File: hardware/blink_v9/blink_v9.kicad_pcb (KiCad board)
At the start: 2 copper layers, 119 x 92 mm, 115 parts, among them J1 Conn_01x02, J11 KH-BNC50-3511, J12 KH-BNC50-3511, J13 KH-BNC50-3511, J14 Conn_02x16_Odd_Even, J15 Conn_01x01, J16 Conn_01x01, J2 PJ-320D, J3 PJ-320D, J4 KH-BNC50-3511, J5 Conn_01x06_Pin, J7 Conn_01x06_Pin, J8 Conn_01x06, J9 USB_C_Receptacle, Q1 S8550, Q2 S8050, SW1 SW_SPDT, SW2 LC1258OASP, SW3 LC1258OASP, SW5 LC1258OASP, U1 AMS1117-3.3, U2 AD8397, U3 M24C02-RMN, U4 STM32F405RGTx, U5 SN74LVC1G14DBV, U6 SN74LVC1G14DBV, U7 CH340C, U8 USBLC6-2P6, U9 MCP73832-2-OT, X1 GTXO-14V (2.048MHz), Y1 16MHz

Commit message: fix up osc footprint
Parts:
- removed J8: Conn_01x06, Connector_JST:JST_PH_S6B-PH-SM4-TB_1x06-1MP_P2.00mm_Horizontal
- added C30: 100n, Capacitor_SMD:C_0402_1005Metric, F.Cu at (166.0, 33.0)
- added J6: Conn_01x03, Connector_JST:JST_PH_S3B-PH-SM4-TB_1x03-1MP_P2.00mm_Horizontal, F.Cu at (170.7, 26.4)
- added R42: 1K0, Resistor_SMD:R_0603_1608Metric, F.Cu at (178.8, 22.0)
- added R43: 1K0, Resistor_SMD:R_0603_1608Metric, F.Cu at (178.8, 24.5)
- added R44: 1K0, Resistor_SMD:R_0603_1608Metric, F.Cu at (178.8, 27.0)
- added R45: 1K0, Resistor_SMD:R_0603_1608Metric, F.Cu at (178.8, 29.5)
- added U10: TMP102xxDRL, Package_TO_SOT_SMD:SOT-563, F.Cu at (178.7, 32.4)
- Q1, Q2: footprint Package_TO_SOT_SMD:SC-59 -> Package_TO_SOT_THT:TO-92_Inline
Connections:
- net SYNC_IN2 renamed AUX_SYNC_IN
- J7 pad 2: /BOOT0 -> Net-(J7-Pin_2)
- J7 pad 3: /BOOT1 -> Net-(J7-Pin_3)
- J7 pad 4: /BTN1 -> Net-(J7-Pin_4)
- J7 pad 5: /DB3 -> Net-(J7-Pin_5)
- R35 pad 2: /BOOT0 -> /AUX_CLK
- U4 pad 42: /NCOL1 -> /USB_RX
- U4 pad 43: /LEDMY -> /USB_TX
- U4 pad 58: /USB_RX -> /NCOL1
- U4 pad 59: /USB_TX -> /LEDMY
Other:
- board text added: "Blink Rev 9.0 Cullen Jennings 2023"
- board text removed: "Blink Rev 8.0 Cullen Jennings 2023"

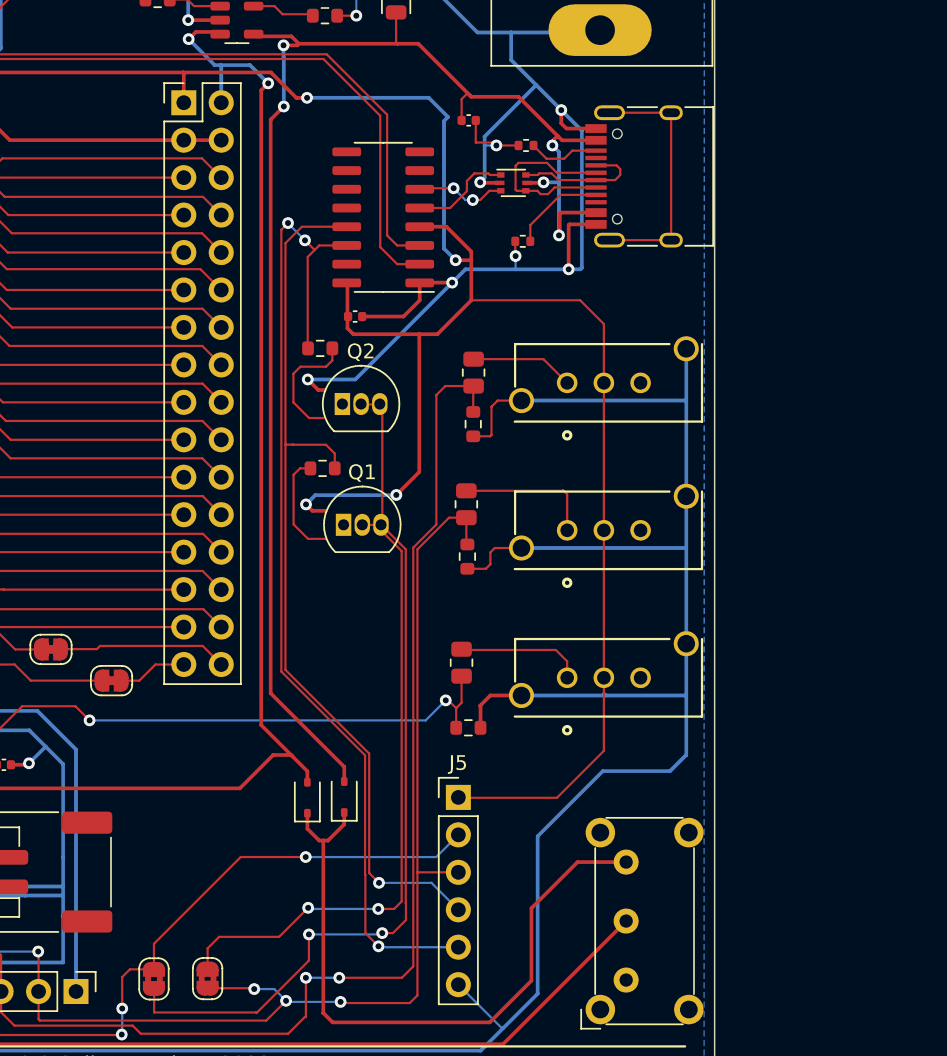
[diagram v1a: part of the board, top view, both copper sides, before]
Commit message: moved switches
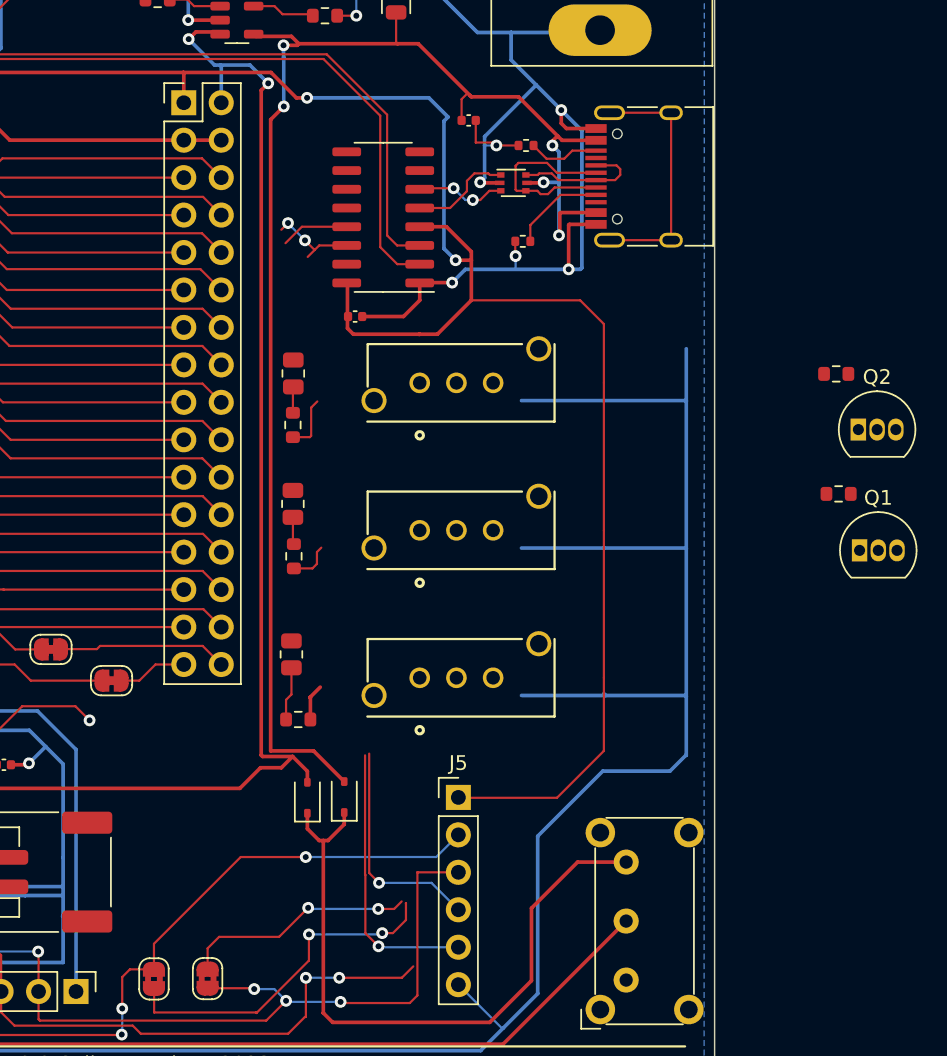
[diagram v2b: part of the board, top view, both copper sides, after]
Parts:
- moved Q1 35.0 mm to (239.8, 91.4)
- moved Q2 35.0 mm to (239.7, 83.2)
- moved R37 35.0 mm to (238.2, 79.4)
- moved R38 35.0 mm to (238.4, 87.5)
- moved R18 12.2 mm to (201.4, 82.9)
- moved R25 12.2 mm to (201.4, 79.4)
- moved R14 11.8 mm to (201.5, 91.8)
- moved R35 11.8 mm to (201.4, 88.2)
- moved R34 11.6 mm to (201.8, 102.8)
- moved R36 11.6 mm to (201.3, 98.4)
- moved SW2 10.0 mm to (210.0, 90.0)
- moved SW3 10.0 mm to (210.0, 100.0)
- moved SW5 10.0 mm to (210.0, 80.0)
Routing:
- net /USB_RTS: track 69.2 -> 25.0 mm
- net /BOOT1: track 126.4 -> 84.3 mm
- net /USB_DTR: track 61.4 -> 19.8 mm
- net Net-(JP3-B): track 59.2 -> 23.5 mm
- net Net-(JP4-B): track 43.2 -> 15.9 mm
- net /BOOT0: track 144.9 -> 118.8 mm
- net /BTN1: track 110.8 -> 85.1 mm, vias 5 -> 4
- net GND: track 1099.5 -> 1080.0 mm, vias 43 -> 42
- net +3.3V: track 507.6 -> 488.1 mm, vias 21 -> 19
- net Net-(R35-Pad1): track 9.41 -> 0.00 mm
- net Net-(R36-Pad1): track 8.62 -> 0.07 mm
- net Net-(Q2-B): track 8.34 -> 0.00 mm
- net Net-(Q1-B): track 7.28 -> 0.00 mm
- net Net-(R25-Pad1): track 7.01 -> 0.00 mm
- net VBUS: track 97.3 -> 99.0 mm
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
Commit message: place parts on v9
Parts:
- Q1, Q2: footprint Package_TO_SOT_THT:TO-92_Inline -> Package_TO_SOT_SMD:SOT-23-3
- X1: footprint blinky_footprints:Oscillator_DIP-14 -> blinky_footprints:OSC_DIP-14
- moved R42 93.6 mm to (177.2, 115.6), turned to -90 degrees
- moved R44 88.8 mm to (174.4, 115.7), turned to -90 degrees
- moved R43 88.0 mm to (175.6, 112.4), turned to -90 degrees
- moved R45 83.2 mm to (173.2, 112.5), turned to -90 degrees
- moved U10 68.5 mm to (158.6, 97.9), turned to 180 degrees
- moved C30 65.6 mm to (156.2, 97.8)
- moved Q1 54.6 mm to (204.5, 49.6)
- moved R38 54.6 mm to (203.1, 45.8)
- moved Q2 53.8 mm to (197.5, 49.8)
- moved R37 53.8 mm to (196.0, 46.0)
- moved J6 23.2 mm to (172.0, 49.5), turned to 180 degrees
- moved J1 2.15 mm to (186.7, 112.7)
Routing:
- net /BOOT1: track 84.3 -> 24.5 mm, vias 4 -> 2
- net Net-(J7-Pin_3): track 0.00 -> 46.3 mm, vias 0 -> 2
- net /DB3: track 54.3 -> 43.3 mm
- net Net-(J7-Pin_2): track 0.00 -> 10.7 mm
- net Net-(J7-Pin_5): track 0.00 -> 10.4 mm
- net /BTN1: track 85.1 -> 76.4 mm
- net GND: track 1080.0 -> 1071.4 mm
- net Net-(J7-Pin_4): track 0.00 -> 8.36 mm
- net Net-(J4-In): track 86.3 -> 92.2 mm
- net +BATT: track 95.1 -> 89.9 mm
- net /SWDCLK: track 42.1 -> 38.8 mm
- net /SWDIO: track 32.5 -> 29.3 mm
- net /USB_RX: track 99.9 -> 97.1 mm
- net +3.3V: track 488.1 -> 485.3 mm
- net +3.3VA: track 115.5 -> 118.1 mm
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
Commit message: add labels blink 9
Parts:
- moved J5 70.0 mm to (179.0, 46.7), turned to 90 degrees
- moved D2 12.1 mm to (213.8, 112.1)
- moved D3 12.1 mm to (216.3, 112.0)
- moved J6 6.72 mm to (165.3, 50.0)
- moved R18 2.60 mm to (204.0, 82.7)
- moved R25 2.60 mm to (204.0, 79.2)
- moved R35 2.21 mm to (203.6, 88.1)
- moved R14 2.21 mm to (203.7, 91.7)
- moved R34 2.12 mm to (203.8, 103.4)
- moved R36 2.12 mm to (203.3, 99.0)
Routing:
- net /USB_RX: track 97.1 -> 46.0 mm, vias 5 -> 1
- net /NCOL1: track 42.1 -> 88.6 mm, vias 0 -> 3
- net Net-(D2-K): track 45.0 -> 16.2 mm
- net /BOOT0: track 118.8 -> 95.9 mm, vias 5 -> 2
- net +3.3V: track 485.3 -> 465.2 mm, vias 19 -> 18
- net /USB_RTS: track 25.0 -> 6.19 mm, vias 3 -> 2
- net /USB_DTR: track 19.8 -> 4.62 mm, vias 1 -> 0
- net /NRST: track 112.5 -> 97.7 mm, vias 7 -> 6
- net VBUS: track 99.0 -> 112.7 mm
- net +BATT: track 89.9 -> 101.6 mm
- net Net-(JP3-B): track 23.5 -> 13.6 mm, vias 2 -> 0
- net Net-(J7-Pin_3): track 46.3 -> 38.7 mm, vias 2 -> 0
- net Net-(JP4-B): track 15.9 -> 9.36 mm, vias 2 -> 0
- net Net-(J4-In): track 92.2 -> 89.5 mm, vias 2 -> 1
- net /SWDIO: track 29.3 -> 27.9 mm, vias 2 -> 1
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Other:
- board text added: "BTN1"
- board text added: "BTN2"
- board text added: "BTN3"
- board text added: "Bat"
- board text added: "Debug"
- board text added: "MIC"
- board text added: "Prog"
- board text added: "SPKR"
- board text added: "SYNC IN"
- board text added: "SYNC OUT"

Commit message: fix up SMD sizes to motly 0603 on blink
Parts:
- C13, C17, C25, C26, C6, C7, C8, C9: footprint Capacitor_SMD:C_0805_2012Metric -> Capacitor_SMD:C_0603_1608Metric
- C28, C29: footprint Capacitor_SMD:C_0402_1005Metric -> Capacitor_SMD:C_0603_1608Metric
- R1, R13, R16, R19, R2, R24, R25, R3, R35, R36, R39, R4, R5, R6, R7, R8: footprint Resistor_SMD:R_0805_2012Metric -> Resistor_SMD:R_0603_1608Metric
- R21, R22: footprint Resistor_SMD:R_0402_1005Metric -> Resistor_SMD:R_0603_1608Metric
- moved R22 0.42 mm to (217.3, 70.2)
- moved R21 0.29 mm to (217.0, 63.7)
- moved C29 0.25 mm to (181.6, 105.9)
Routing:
- net (no net): track 0.00 -> 16.4 mm
- net GND: track 1070.3 -> 1075.0 mm
- net +BATT: track 101.6 -> 105.0 mm
- net Net-(U7-UD+): track 6.93 -> 8.54 mm
- net Net-(J9-CC1): track 6.40 -> 5.88 mm
- net Net-(U7-UD-): track 6.12 -> 5.68 mm, vias 2 -> 0

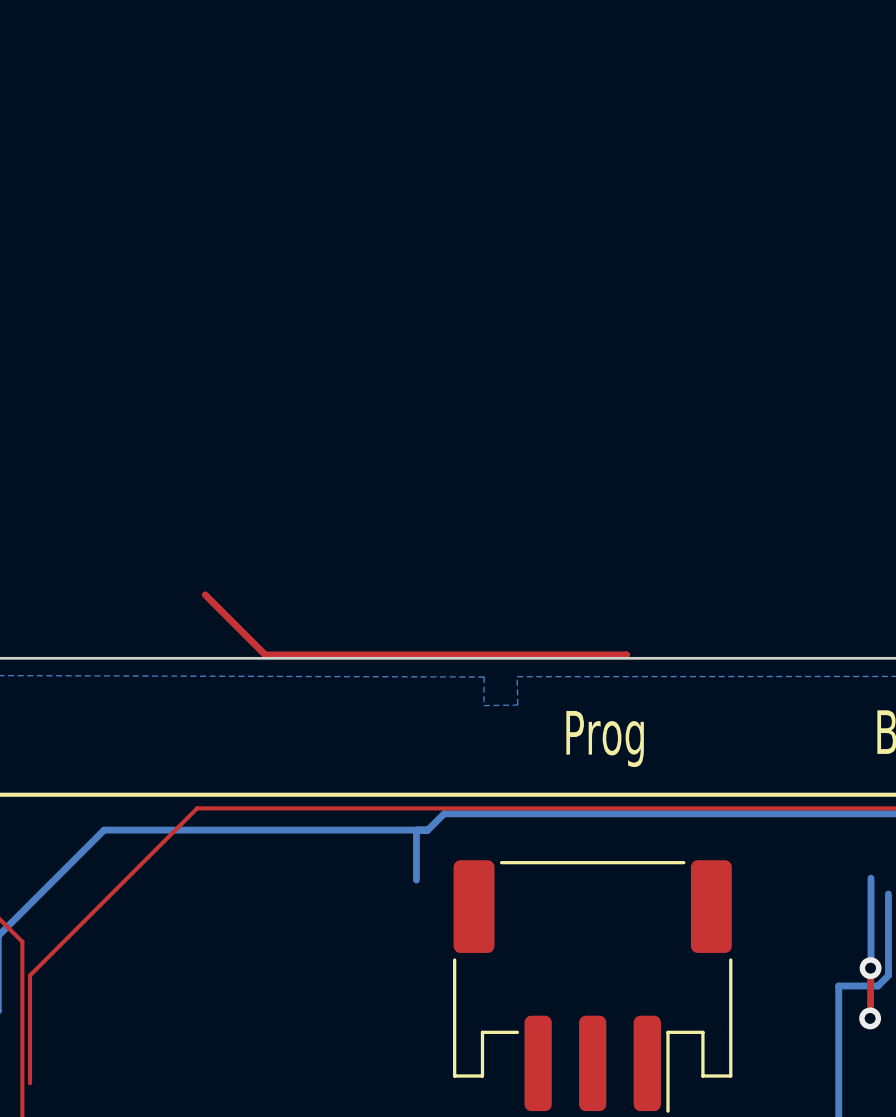
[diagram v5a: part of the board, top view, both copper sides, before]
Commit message: add RGB led
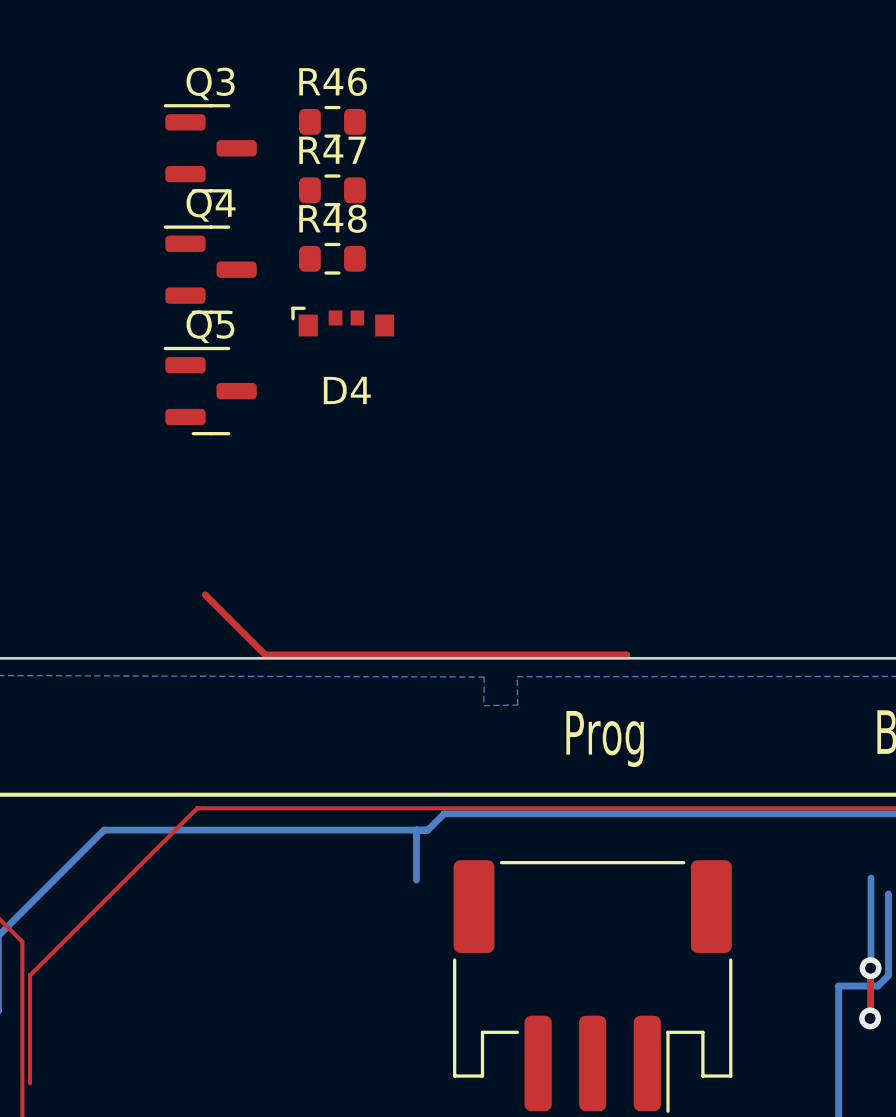
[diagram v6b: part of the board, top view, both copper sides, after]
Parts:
- added D4: LED_ABGR, blinky_footprints:LED_RGB_MHS110FRGBCT, F.Cu at (156.3, 26.4)
- added Q3: 2N7002, Package_TO_SOT_SMD:SOT-23, F.Cu at (151.3, 19.3)
- added Q4: 2N7002, Package_TO_SOT_SMD:SOT-23, F.Cu at (151.3, 23.8)
- added Q5: 2N7002, Package_TO_SOT_SMD:SOT-23, F.Cu at (151.3, 28.2)
- added R46: 150R, Resistor_SMD:R_0603_1608Metric, F.Cu at (155.8, 18.3)
- added R47: 47R, Resistor_SMD:R_0603_1608Metric, F.Cu at (155.8, 20.8)
- added R48: 47R, Resistor_SMD:R_0603_1608Metric, F.Cu at (155.8, 23.4)
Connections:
- R25 pad 1: Net-(R25-Pad1) -> /BOOT1

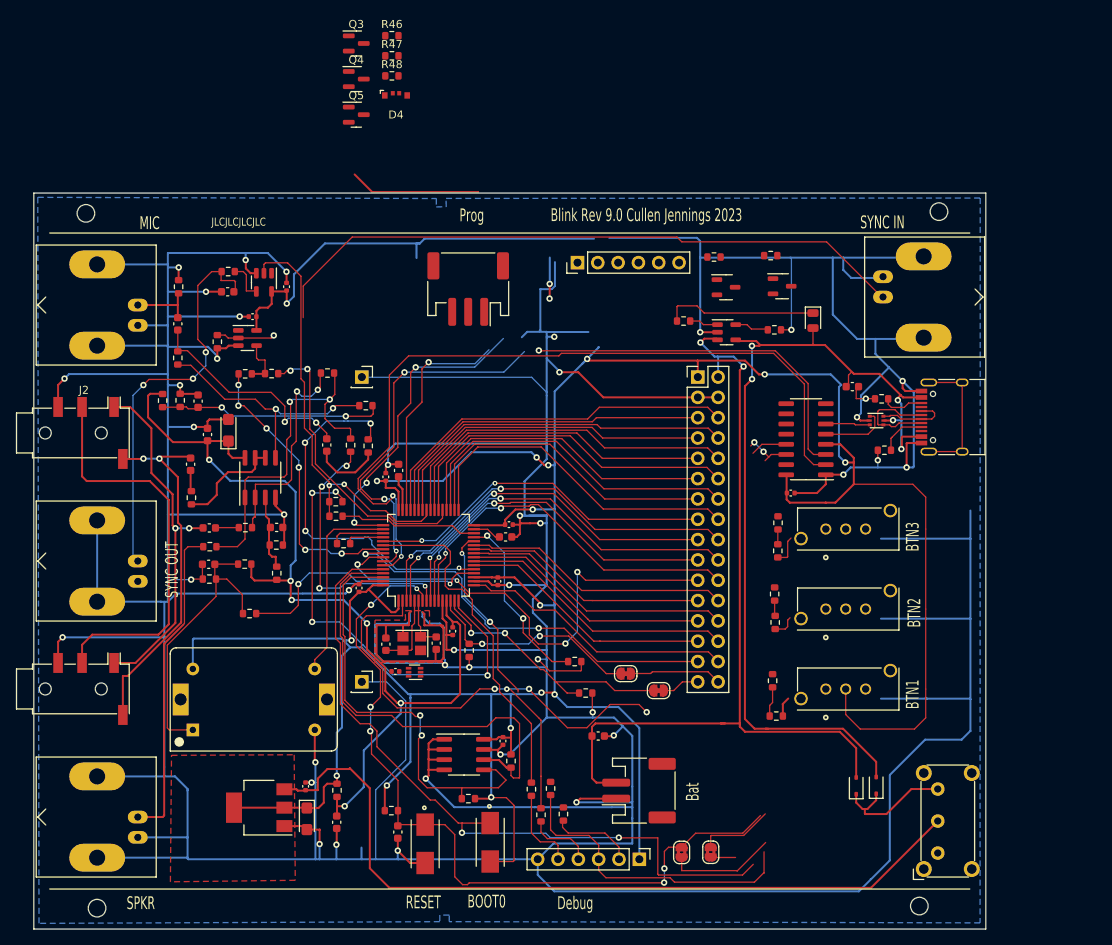
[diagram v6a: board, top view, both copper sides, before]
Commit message: new footprints and symbols for new switch
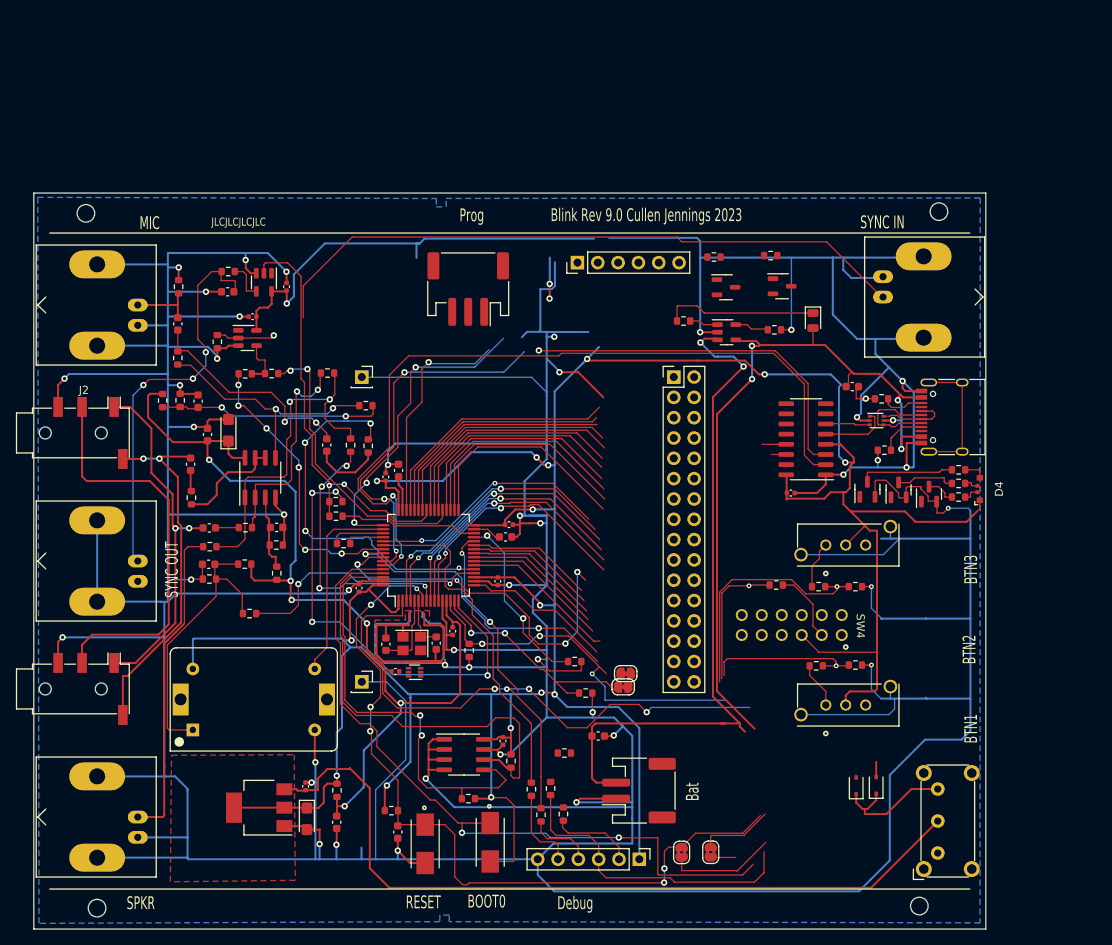
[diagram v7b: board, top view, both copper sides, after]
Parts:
- removed SW2: LC1258OASP, blinky_footprints:LC1258OASP
- added SW4: SW_Push_4PDT, blinky_footprints:PBH4UOANAGX, F.Cu at (212.0, 93.2)
- moved R46 89.2 mm to (226.6, 72.6)
- moved R47 88.7 mm to (226.6, 74.3)
- moved R48 88.3 mm to (226.6, 76.0), turned to 180 degrees
- moved D4 88.2 mm to (229.8, 75.0), turned to 90 degrees
- moved Q5 85.9 mm to (222.9, 75.6), turned to 90 degrees
- moved Q4 85.0 mm to (219.1, 75.1), turned to 90 degrees
- moved Q3 84.8 mm to (215.2, 75.0), turned to 90 degrees
- moved R14 31.0 mm to (177.3, 108.0), turned to 0 degrees
- moved R34 11.8 mm to (213.7, 97.0)
- moved R18 10.7 mm to (213.7, 87.2), turned to 180 degrees
- moved R25 9.45 mm to (209.1, 87.2), turned to 0 degrees
- moved R36 5.76 mm to (208.8, 97.1), turned to 0 degrees
- moved JP1 4.45 mm to (184.7, 99.7)
- moved J14 3.00 mm to (191.0, 61.0)
- moved SW3 2.00 mm to (210.0, 102.0)
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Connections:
- R25 pad 1: /BOOT1 -> Net-(R25-Pad1)
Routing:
- net /LEDMY: track 45.5 -> 0.00 mm
- net /NCOL1: track 88.6 -> 46.4 mm
- net GND: track 1075.0 -> 1112.1 mm, vias 41 -> 44
- net /AUX_CLK: track 27.6 -> 63.2 mm, vias 2 -> 4
- net /USB_RX: track 46.0 -> 76.2 mm
- net /USB_TX: track 98.9 -> 128.6 mm
- net /BTN1: track 76.4 -> 105.7 mm, vias 4 -> 5
- net /BOOT1: track 24.5 -> 53.6 mm, vias 2 -> 3
- net +BATT: track 105.0 -> 86.9 mm
- net /LED10: track 33.4 -> 15.8 mm
- net /LED8: track 34.0 -> 17.1 mm
- net (no net): track 16.4 -> 0.00 mm
- net /LED2: track 34.7 -> 18.5 mm
- net /NCOL10: track 50.3 -> 34.4 mm
- net /LED4: track 34.5 -> 18.8 mm
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
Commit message: update rough routing
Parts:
- moved R14 10.1 mm to (171.2, 116.0), turned to 90 degrees
- moved R38 2.84 mm to (200.4, 45.0), turned to 180 degrees
- moved Q1 2.20 mm to (202.3, 49.4), turned to -90 degrees
- moved Q5 1.25 mm to (222.3, 74.5)
- moved Q3 1.25 mm to (214.6, 73.9)
- moved Q4 1.25 mm to (218.5, 74.0)
- moved R37 1.06 mm to (195.7, 45.0)
- moved Q2 0.25 mm to (197.4, 49.5), turned to -90 degrees
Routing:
- net /USB_TX: track 128.6 -> 74.4 mm
- net /NCOL1: track 46.4 -> 0.00 mm, vias 3 -> 0
- net /LEDMG: track 30.4 -> 74.8 mm, vias 0 -> 1
- net /LED10: track 15.8 -> 59.9 mm, vias 0 -> 2
- net Net-(JP3-B): track 13.6 -> 55.9 mm, vias 0 -> 1
- net Net-(JP4-B): track 9.36 -> 51.1 mm, vias 0 -> 1
- net /LEDMR: track 31.8 -> 72.6 mm, vias 0 -> 1
- net /LED9: track 16.4 -> 53.5 mm, vias 0 -> 2
- net /BOOT0: track 94.0 -> 131.0 mm, vias 2 -> 3
- net /LEDMY: track 0.00 -> 34.4 mm, vias 0 -> 1
- net /BOOT1: track 53.6 -> 85.0 mm, vias 3 -> 5
- net /USB_RTS: track 1.87 -> 31.2 mm, vias 0 -> 2
- net /NRST: track 97.7 -> 125.1 mm, vias 6 -> 8
- net Net-(J7-Pin_3): track 38.7 -> 12.9 mm
- net /USB_DTR: track 3.04 -> 28.5 mm, vias 0 -> 2
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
